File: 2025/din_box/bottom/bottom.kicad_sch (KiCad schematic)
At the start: 35 parts, among them J1 PWR, J2 RS485_Modbus_BAC, J3 Conn_02x02_Odd_Even, J4 RLY, J5 PROG, K1 G6K-2, Q1 2N7002, U1 CH32V003JxMx, U2 SSP3085, U3 ME6209A50M3G

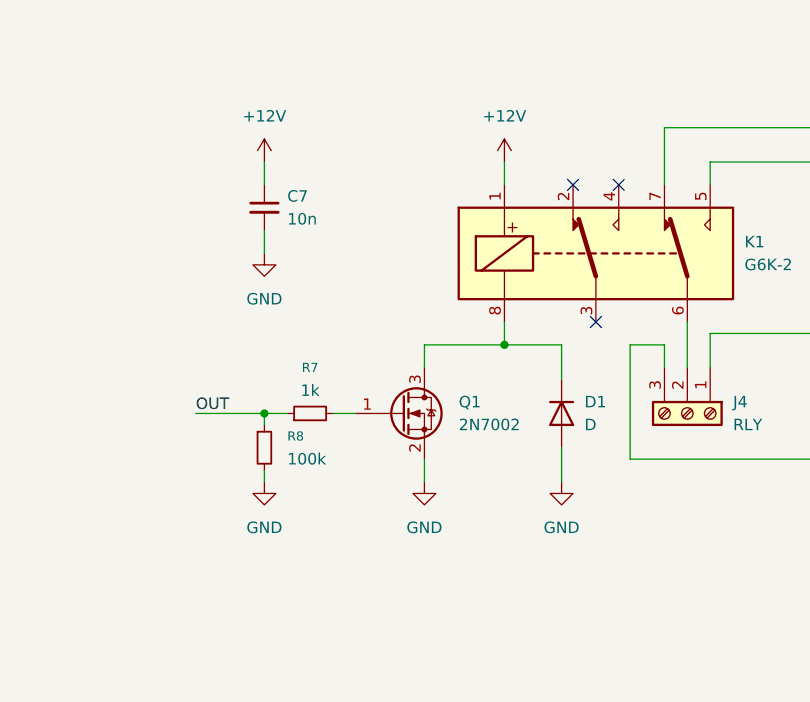
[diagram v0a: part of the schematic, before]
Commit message: Adding USB-C to RS485 converter board
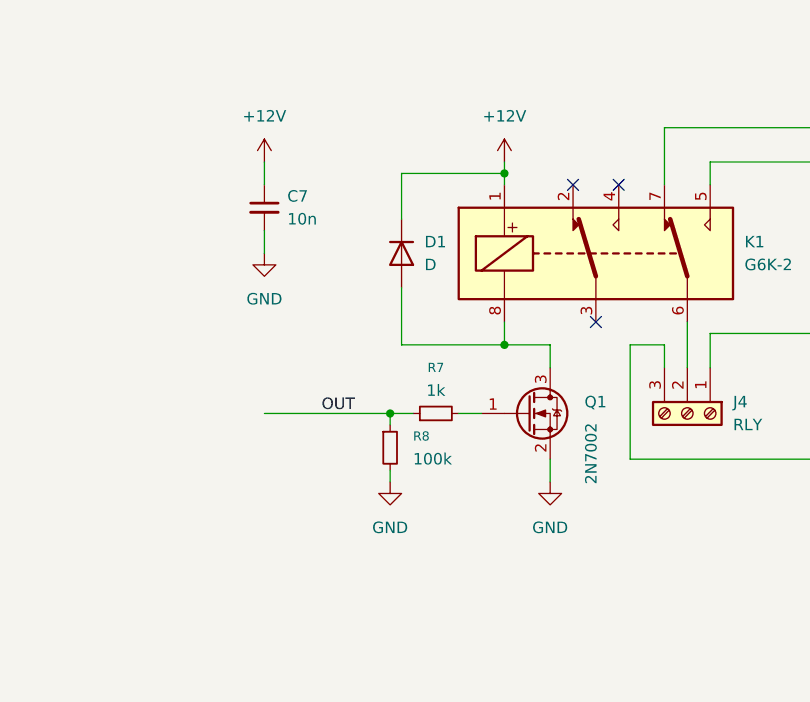
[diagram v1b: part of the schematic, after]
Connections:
- net +12V: now also D1.1 (K)
- net GND: no longer D1.2 (A)
- net at K1.8, Q1.3 (D): now also D1.2 (A); no longer D1.1 (K)
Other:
- moved on the sheet: D1, Q1, R7, R8
